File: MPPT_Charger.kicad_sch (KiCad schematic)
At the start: 114 parts, among them J1 Solar, J2 Battery, J3 USB_B_Mini, J4 INTERFACE PORT, J6 JTAG, J8 Micro_SD_Card_Det_Hirose_DM3AT, J9 IIC RTC, Q1 CSD19505KCS, Q11 CSD19505KCS, Q12 CSD19505KCS, Q13 CSD19505KCS, Q2 CSD19505KCS, Q3 CSD19505KCS, Q4 Si2306, Q5 MMBT3904 1A, Q6 MMBT3904 1A, Q7 Si2306, U1 ACS712, U10 ADS1015, U2 B1212S, U3 AMS1117-5.0, U4 AMS1117-3.3, U5 XL7005A, U6 XL7005A, U7 IR2104, U8 ESP32, U9 CH340G

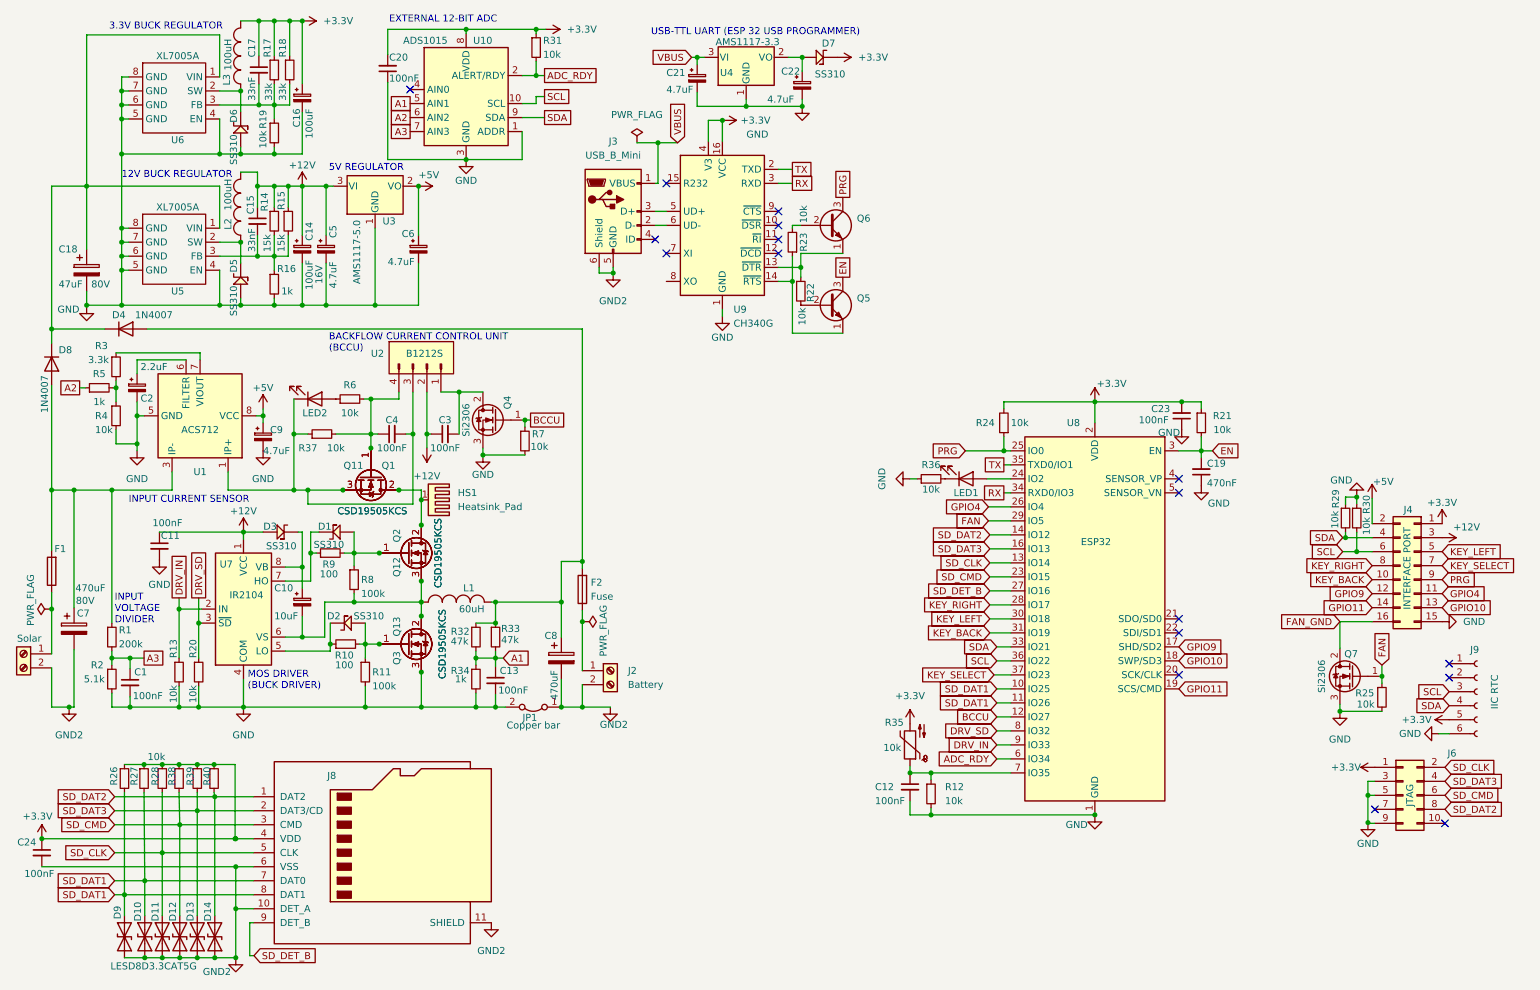
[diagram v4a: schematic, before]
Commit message: SD card pins were wrong https://github.com/MarcelMo/MPPT_Kicad_Schematics/issues/1
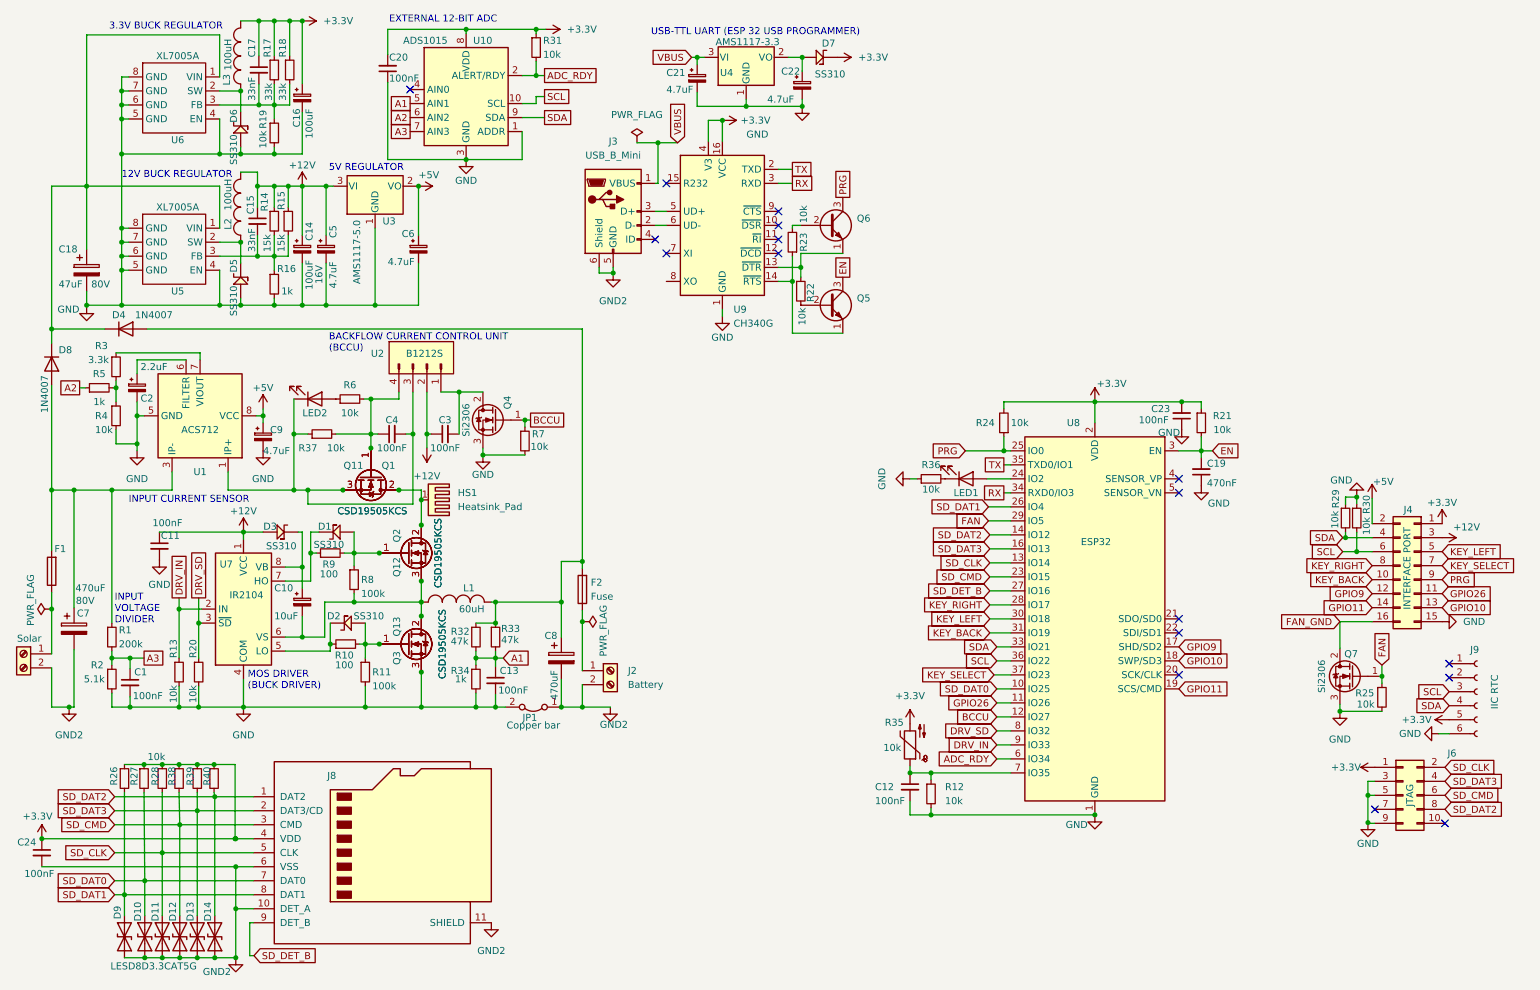
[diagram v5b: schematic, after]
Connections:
- net SD_DAT1: now also U8.26 (IO4); no longer D10.2 (A2), J8.7 (DAT0), R27.2, U8.10 (IO25), U8.11 (IO26)
- net GPIO4 renamed GPIO26
- net GPIO26: now also U8.11 (IO26); no longer U8.26 (IO4)
- new net SD_DAT0: D10.2 (A2), J8.7 (DAT0), R27.2, U8.10 (IO25)

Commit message: Some missing copper and minor changes
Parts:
- C14: reichelt item (none) -> VF 100/25 P-D8
- C16: reichelt item (none) -> PAN 16SVPC100M
- C5: footprint Capacitor_SMD:C_0603_1608Metric -> Capacitor_SMD:C_0805_2012Metric; reichelt item (none) -> KEM X5R0805 4,7U
- C7, C8: reichelt item (none) -> FC-A 470U 100 / RAD FC 470/50
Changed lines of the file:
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@@
+      (effects (font (size 1.27 1.27)) hide)
+    )
+    (property "reichelt item" "FC-A 470U 100 / RAD FC 470/50" (id 4) (at 112.776 130.302 0)
       (effects (font (size 1.27 1.27)) hide)
     )
@@
     )
     (property "Voltage" "80V" (id 4) (at 26.416 119.888 0))
+    (property "reichelt item" "FC-A 470U 100 / RAD FC 470/50" (id 5) (at 24.384 124.968 0)
+      (effects (font (size 1.27 1.27)) hide)
+    )
     (pin "1")
     (pin "2")
@@
     )
     (property "Voltage" "16V" (id 4) (at 68.834 60.706 90))
+    (property "reichelt item" "VF 100/25 P-D8" (id 5) (at 65.786 56.134 90)
+      (effects (font (size 1.27 1.27)) hide)
+    )
     (pin "1")
     (pin "2")
@@
       (effects (font (size 1.27 1.27)) (justify left))
     )
-    (property "Footprint" "Capacitor_SMD:C_0603_1608Metric" (id 2) (at 70.104 56.134 0)
+    (property "Footprint" "Capacitor_SMD:C_0805_2012Metric" (id 2) (at 70.104 56.134 0)
       (effects (font (size 1.27 1.27)) hide)
     )
     (property "Datasheet" "~" (id 3) (at 70.104 56.134 0)
+      (effects (font (size 1.27 1.27)) hide)
+    )
+    (property "reichelt item" "KEM X5R0805 4,7U" (id 4) (at 70.104 56.134 90)
       (effects (font (size 1.27 1.27)) hide)
     )
@@
       (effects (font (size 1.27 1.27)) hide)
     )
+    (property "reichelt item" "PAN 16SVPC100M" (id 4) (at 65.786 28.702 90)
+      (effects (font (size 1.27 1.27)) hide)
+    )
     (pin "1")
     (pin "2")
@@
     )
     (path "/933431dd-ef15-454c-85eb-5edf224d3885"
-      (reference "C5") (unit 1) (value "4.7uF") (footprint "Capacitor_SMD:C_0603_1608Metric")
+      (reference "C5") (unit 1) (value "4.7uF") (footprint "Capacitor_SMD:C_0805_2012Metric")
     )
     (path "/6f750778-f388-4532-b503-a47af89197b5"
